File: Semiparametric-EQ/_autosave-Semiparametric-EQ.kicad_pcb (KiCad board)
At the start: 2 copper layers, 100 x 100 mm, 52 parts, among them J1 Conn_01x05_Male, J2 Conn_01x02_Male, SW1 Peak/Shelf, U1 NE5532, U2 TL072, U3 NE5532

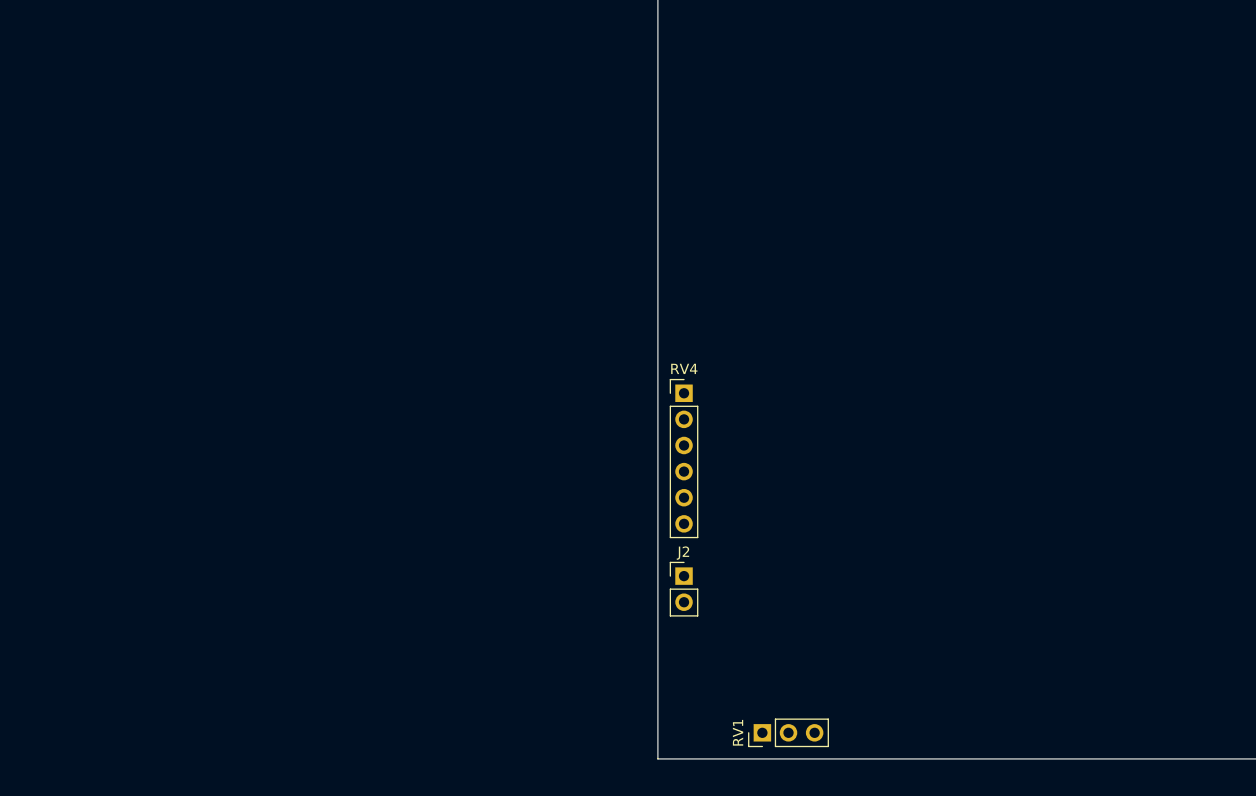
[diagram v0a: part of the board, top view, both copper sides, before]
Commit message: Added bulk caps, started eq board layout
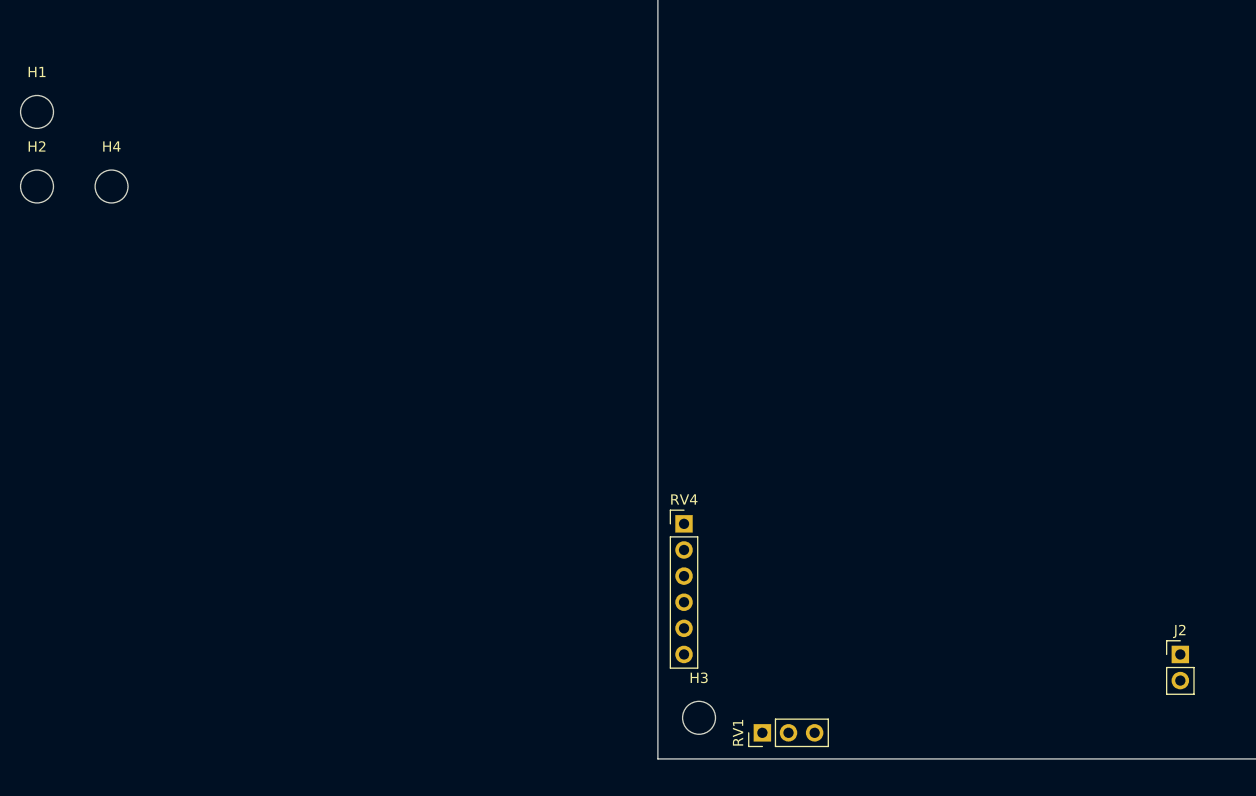
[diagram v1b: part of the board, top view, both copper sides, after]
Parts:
- added H1: MountingHole, MountingHole:MountingHole_3.2mm_M3_ISO7380, F.Cu at (-60.4, -62.9)
- added H2: MountingHole, MountingHole:MountingHole_3.2mm_M3_ISO7380, F.Cu at (-60.4, -55.7)
- added H3: MountingHole, MountingHole:MountingHole_3.2mm_M3_ISO7380, F.Cu at (4.00, -4.00)
- added H4: MountingHole, MountingHole:MountingHole_3.2mm_M3_ISO7380, F.Cu at (-53.1, -55.7)
- moved J2 48.9 mm to (50.8, -10.2)
- moved RV4 12.7 mm to (2.54, -22.9)
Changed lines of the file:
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@@
     (tracks 5)
     (zones 0)
-    (modules 52)
+    (modules 56)
     (nets 35)
   )
@@
   )
   (module Connector_PinHeader_2.54mm:PinHeader_1x02_P2.54mm_Vertical (layer F.Cu)
-    (at 2.54 -17.78)
+    (at 50.8 -10.16)
     (descr "Through hole straight pin header, 1x02, 2.54mm pitch, single row")
     (tags "Through hole pin header THT 1x02 2.54mm single row")
@@
   )
   (module Connector_PinHeader_2.54mm:PinHeader_1x06_P2.54mm_Vertical (layer F.Cu)
-    (at 2.54 -35.56)
+    (at 2.54 -22.86)
     (descr "Through hole straight pin header, 1x06, 2.54mm pitch, single row")
     (tags "Through hole pin header THT 1x06 2.54mm single row")
@@
     )
   )
+  (module MountingHole:MountingHole_3.2mm_M3_ISO7380 (layer F.Cu)
+    (at -60.374999 -62.914999)
+    (descr "Mounting Hole 3.2mm, no annular, M3, ISO7380")
+    (tags "mounting hole 3.2mm no annular m3 iso7380")
+    (attr virtual)
+    (fp_text reference H1 (at 0 -3.85) (layer F.SilkS)
+      (effects (font (size 1 1) (thickness 0.15)))
+    )
+    (fp_text value MountingHole (at 0 3.85) (layer F.Fab)
+      (effects (font (size 1 1) (thickness 0.15)))
+    )
+    (fp_circle (center 0 0) (end 3.1 0) (layer F.CrtYd) (width 0.05))
+    (fp_circle (center 0 0) (end 2.85 0) (layer Cmts.User) (width 0.15))
+    (fp_text user %R (at 0.3 0) (layer F.Fab)
+      (effects (font (size 1 1) (thickness 0.15)))
+    )
+    (pad 1 np_thru_hole circle (at 0 0) (size 3.2 3.2) (drill 3.2) (layers *.Cu *.Mask))
+  )
+  (module MountingHole:MountingHole_3.2mm_M3_ISO7380 (layer F.Cu)
+    (at -60.374999 -55.664999)
+    (descr "Mounting Hole 3.2mm, no annular, M3, ISO7380")
+    (tags "mounting hole 3.2mm no annular m3 iso7380")
+    (attr virtual)
+    (fp_text reference H2 (at 0 -3.85) (layer F.SilkS)
+      (effects (font (size 1 1) (thickness 0.15)))
+    )
+    (fp_text value MountingHole (at 0 3.85) (layer F.Fab)
+      (effects (font (size 1 1) (thickness 0.15)))
+    )
+    (fp_text user %R (at 0.3 0) (layer F.Fab)
+      (effects (font (size 1 1) (thickness 0.15)))
+    )
+    (fp_circle (center 0 0) (end 2.85 0) (layer Cmts.User) (width 0.15))
+    (fp_circle (center 0 0) (end 3.1 0) (layer F.CrtYd) (width 0.05))
+    (pad 1 np_thru_hole circle (at 0 0) (size 3.2 3.2) (drill 3.2) (layers *.Cu *.Mask))
+  )
+  (module MountingHole:MountingHole_3.2mm_M3_ISO7380 (layer F.Cu)
+    (at 4 -4)
+    (descr "Mounting Hole 3.2mm, no annular, M3, ISO7380")
+    (tags "mounting hole 3.2mm no annular m3 iso7380")
+    (attr virtual)
+    (fp_text reference H3 (at 0 -3.85) (layer F.SilkS)
+      (effects (font (size 1 1) (thickness 0.15)))
+    )
+    (fp_text value MountingHole (at 0 3.85) (layer F.Fab)
+      (effects (font (size 1 1) (thickness 0.15)))
+    )
+    (fp_circle (center 0 0) (end 3.1 0) (layer F.CrtYd) (width 0.05))
+    (fp_circle (center 0 0) (end 2.85 0) (layer Cmts.User) (width 0.15))
+    (fp_text user %R (at 0.3 0) (layer F.Fab)
+      (effects (font (size 1 1) (thickness 0.15)))
+    )
+    (pad 1 np_thru_hole circle (at 0 0) (size 3.2 3.2) (drill 3.2) (layers *.Cu *.Mask))
+  )
+  (module MountingHole:MountingHole_3.2mm_M3_ISO7380 (layer F.Cu)
+    (at -53.124999 -55.664999)
+    (descr "Mounting Hole 3.2mm, no annular, M3, ISO7380")
+    (tags "mounting hole 3.2mm no annular m3 iso7380")
+    (attr virtual)
+    (fp_text reference H4 (at 0 -3.85) (layer F.SilkS)
+      (effects (font (size 1 1) (thickness 0.15)))
+    )
+    (fp_text value MountingHole (at 0 3.85) (layer F.Fab)
+      (effects (font (size 1 1) (thickness 0.15)))
+    )
+    (fp_text user %R (at 0.3 0) (layer F.Fab)
+      (effects (font (size 1 1) (thickness 0.15)))
+    )
+    (fp_circle (center 0 0) (end 2.85 0) (layer Cmts.User) (width 0.15))
+    (fp_circle (center 0 0) (end 3.1 0) (layer F.CrtYd) (width 0.05))
+    (pad 1 np_thru_hole circle (at 0 0) (size 3.2 3.2) (drill 3.2) (layers *.Cu *.Mask))
+  )
   (gr_line (start 0 -100) (end 0 0) (layer Edge.Cuts) (width 0.05))
   (gr_line (start 100 -100) (end 0 -100) (layer Edge.Cuts) (width 0.05))
   (gr_line (start 100 0) (end 100 -100) (layer Edge.Cuts) (width 0.05))
   (gr_line (start 0 0) (end 100 0) (layer Edge.Cuts) (width 0.05))
-  (segment (start -42.055 23.475) (end -41.88 23.3) (width 0.75) (layer B.Cu) (net 1))
-  (segment (start -44.3 23.475) (end -42.055 23.475) (width 0.75) (layer B.Cu) (net 1))
-  (segment (start -49.495 30.925) (end -49.5 30.92) (width 0.75) (layer B.Cu) (net 3))
-  (segment (start -47.1 30.925) (end -49.495 30.925) (width 0.75) (layer B.Cu) (net 3))
-  (segment (start -49.5 25.84) (end -49.5 23.3) (width 0.75) (layer B.Cu) (net 22))
+  (segment (start -42.055 23.475) (end -41.88 23.3) (width 0.75) (layer B.Cu) (net 1) (status 30))
+  (segment (start -44.3 23.475) (end -42.055 23.475) (width 0.75) (layer B.Cu) (net 1) (status 30))
+  (segment (start -49.495 30.925) (end -49.5 30.92) (width 0.75) (layer B.Cu) (net 3) (status 30))
+  (segment (start -47.1 30.925) (end -49.495 30.925) (width 0.75) (layer B.Cu) (net 3) (status 30))
+  (segment (start -49.5 25.84) (end -49.5 23.3) (width 0.75) (layer B.Cu) (net 22) (status 30))
 )
